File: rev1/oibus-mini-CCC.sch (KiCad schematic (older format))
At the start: 84 parts, among them J1 Conn_01x04_Female, J2 USB_B_Micro, J3 uavcan_5pins, J4 Conn_01x02_Female, P1 TC2030-MCP, Q1 DMG3415U-7, Q2 NMOS, Q3 NMOS, SW1 SW_Push, U1 AP2112K-3.3, U10 TPD3E001DRLR, U2 SAM-M8Q, U3 NINA-B311-00B, U4 MCP73831-2-OT, U5 MCP1624T, U6 SHT31-DIS-B, U7 TCAN330, U8 STM32F303CCTx, U9 DW01C-G, Y1 16M, Y2 32kHz

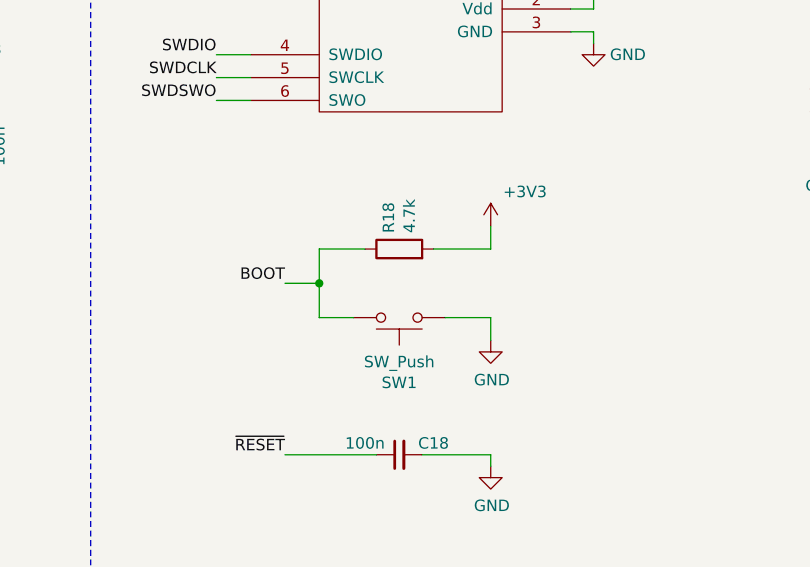
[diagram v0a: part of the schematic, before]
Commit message: corrected the boot pin voltage level
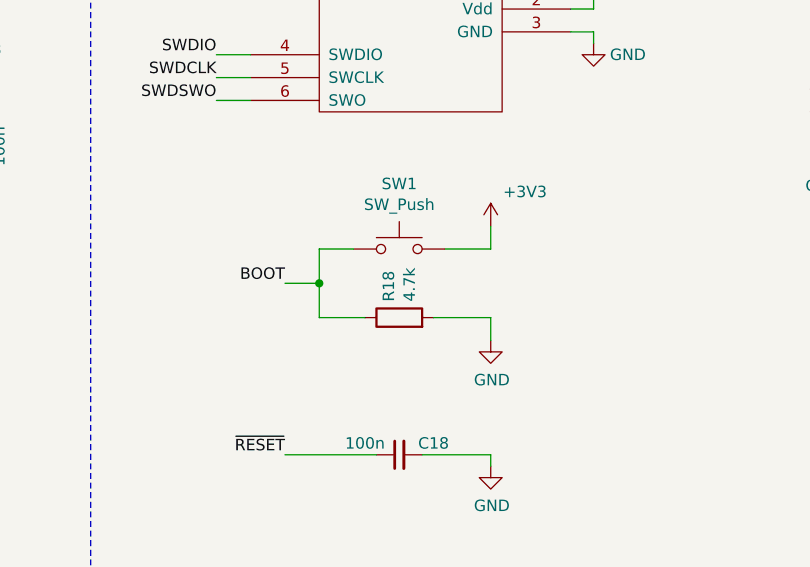
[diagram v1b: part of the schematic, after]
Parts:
- C4, C7, C8: footprint Capacitor_SMD:C_0805_2012Metric -> Capacitor_SMD:C_0603_1608Metric; MPN (none) -> CL10A475KA8NQNC
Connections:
- net +3V3: now also SW1.2; no longer R18.2
- net GND: now also R18.2; no longer SW1.2
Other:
- moved on the sheet: R18, SW1
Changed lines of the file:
@@
 L Switch:SW_Push SW1
 U 1 1 5DAA00C5
-P 8900 2550
-F 0 "SW1" H 8900 2835 50  0000 C CNN
-F 1 "SW_Push" H 8900 2744 50  0000 C CNN
-F 2 "Button_Switch_SMD:SW_SPST_B3U-1000P" H 8900 2750 50  0001 C CNN
-F 3 "~" H 8900 2750 50  0001 C CNN
-	1    8900 2550
-	1    0    0    1
+P 8900 2250
+F 0 "SW1" H 8900 2535 50  0000 C CNN
+F 1 "SW_Push" H 8900 2444 50  0000 C CNN
+F 2 "Button_Switch_SMD:SW_SPST_B3U-1000P" H 8900 2450 50  0001 C CNN
+F 3 "~" H 8900 2450 50  0001 C CNN
+	1    8900 2250
+	1    0    0    -1
 $EndComp
 $Comp
@@
 F 0 "C8" H 5935 8654 50  0000 R CNN
 F 1 "4u7" H 5935 8745 50  0000 R CNN
-F 2 "Capacitor_SMD:C_0805_2012Metric" H 6088 8550 50  0001 C CNN
+F 2 "Capacitor_SMD:C_0603_1608Metric" H 6088 8550 50  0001 C CNN
 F 3 "~" H 6050 8700 50  0001 C CNN
+F 4 "CL10A475KA8NQNC" H 0   0   50  0001 C CNN "MPN"
 	1    6050 8700
 	-1   0    0    1
@@
 F 0 "C7" H 5835 7954 50  0000 R CNN
 F 1 "4u7" H 5835 8045 50  0000 R CNN
-F 2 "Capacitor_SMD:C_0805_2012Metric" H 5988 7850 50  0001 C CNN
+F 2 "Capacitor_SMD:C_0603_1608Metric" H 5988 7850 50  0001 C CNN
 F 3 "~" H 5950 8000 50  0001 C CNN
+F 4 "CL10A475KA8NQNC" H 0   0   50  0001 C CNN "MPN"
 	1    5950 8000
 	0    -1   -1   0
@@
 F 0 "C4" H 4285 10404 50  0000 R CNN
 F 1 "4u7" H 4285 10495 50  0000 R CNN
-F 2 "Capacitor_SMD:C_0805_2012Metric" H 4438 10300 50  0001 C CNN
+F 2 "Capacitor_SMD:C_0603_1608Metric" H 4438 10300 50  0001 C CNN
 F 3 "~" H 4400 10450 50  0001 C CNN
+F 4 "CL10A475KA8NQNC" H 0   0   50  0001 C CNN "MPN"
 	1    4400 10450
 	-1   0    0    1
@@
 L Device:R R18
 U 1 1 5E02E367
-P 8900 2250
-F 0 "R18" H 8970 2296 50  0000 L CNN
-F 1 "4.7k" H 8970 2205 50  0000 L CNN
-F 2 "Resistor_SMD:R_0603_1608Metric" V 8830 2250 50  0001 C CNN
-F 3 "~" H 8900 2250 50  0001 C CNN
-F 4 "" H -6350 -1500 50  0001 C CNN "MPN"
-	1    8900 2250
+P 8900 2550
+F 0 "R18" H 8970 2596 50  0000 L CNN
+F 1 "4.7k" H 8970 2505 50  0000 L CNN
+F 2 "Resistor_SMD:R_0603_1608Metric" V 8830 2550 50  0001 C CNN
+F 3 "~" H 8900 2550 50  0001 C CNN
+F 4 "" H -6350 -1200 50  0001 C CNN "MPN"
+	1    8900 2550
 	0    -1   -1   0
 $EndComp
@@
 	8550 2400 8550 2250
 Wire Wire Line
-	8550 2250 8750 2250
+	8550 2250 8700 2250
 Wire Wire Line
 	8550 2400 8550 2550
-Wire Wire Line
-	8550 2550 8700 2550
 Connection ~ 8550 2400
-Wire Wire Line
-	9050 2250 9300 2250
 Wire Wire Line
 	9300 2250 9300 2150
@@
 NoConn ~ 5300 1700
 Wire Wire Line
-	9300 2550 9100 2550
-Wire Wire Line
 	8400 3150 8800 3150
 Wire Wire Line
@@
 Wire Wire Line
 	13700 8650 13900 8650
+Wire Wire Line
+	9100 2250 9300 2250
+Wire Wire Line
+	9050 2550 9300 2550
+Wire Wire Line
+	8550 2550 8750 2550
 $EndSCHEMATC

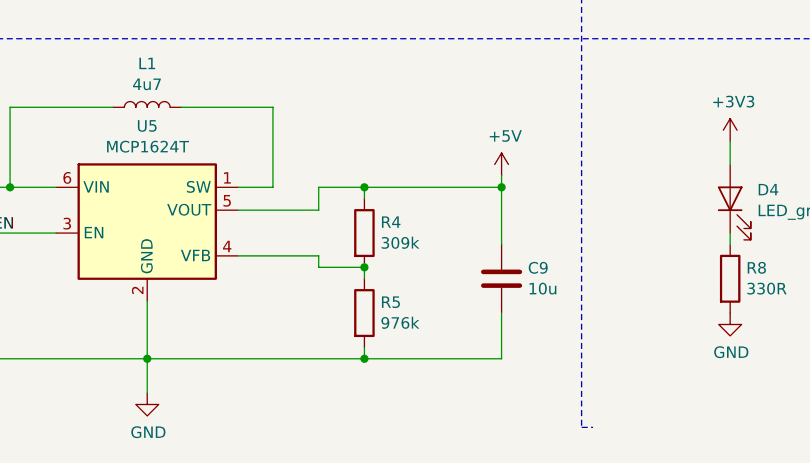
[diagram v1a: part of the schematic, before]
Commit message: changed part value where necessary, added MPN where needed, created BOM, created bare code
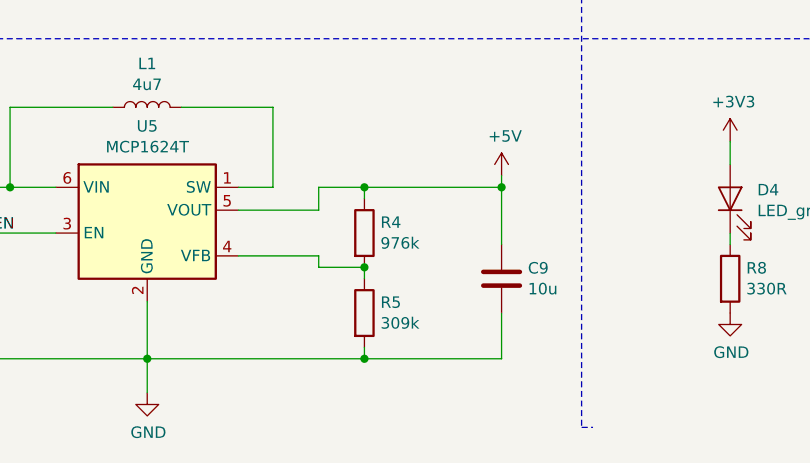
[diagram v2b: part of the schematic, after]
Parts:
- D7: LCSC (none) -> C264607
- R4: value 309k -> 976k
- R5: value 976k -> 309k
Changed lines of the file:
@@
 P 6600 10350
 F 0 "R4" H 6670 10396 50  0000 L CNN
-F 1 "309k" H 6670 10305 50  0000 L CNN
+F 1 "976k" H 6670 10305 50  0000 L CNN
 F 2 "Resistor_SMD:R_0603_1608Metric" V 6530 10350 50  0001 C CNN
 F 3 "~" H 6600 10350 50  0001 C CNN
@@
 P 6600 10700
 F 0 "R5" H 6670 10746 50  0000 L CNN
-F 1 "976k" H 6670 10655 50  0000 L CNN
+F 1 "309k" H 6670 10655 50  0000 L CNN
 F 2 "Resistor_SMD:R_0603_1608Metric" V 6530 10700 50  0001 C CNN
 F 3 "~" H 6600 10700 50  0001 C CNN
@@
 F 3 "~" H 6150 3550 50  0001 C CNN
 F 4 "150141M173100" H 6150 3600 50  0001 C CNN "MPN"
+F 5 "C264607" H 6150 3600 50  0001 C CNN "LCSC"
 	1    6150 3600
 	1    0    0    -1
